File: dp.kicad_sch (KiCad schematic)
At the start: 27 parts, among them J1 DisplayPort_Molex_472720001, U1 74AVC4T245_UQFN, U2 FIN1019MTC, U3 TPD4E05U06QDQARQ1, U4 824012823

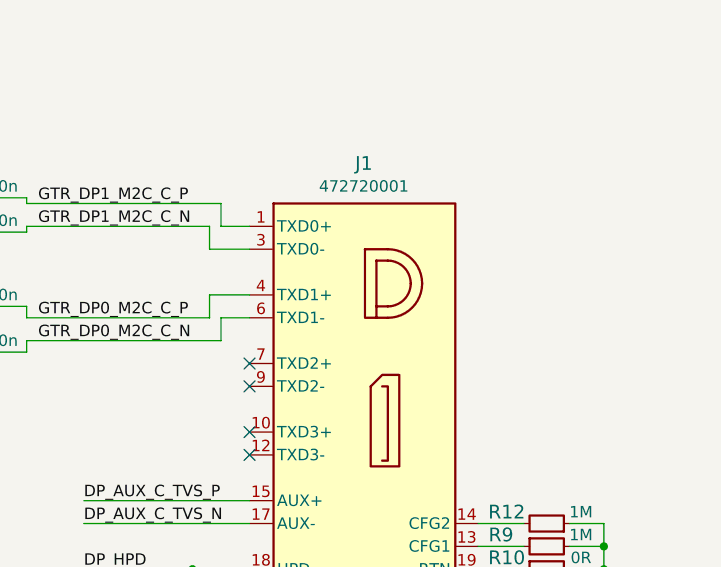
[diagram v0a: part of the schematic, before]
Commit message: removed PoE from schematic
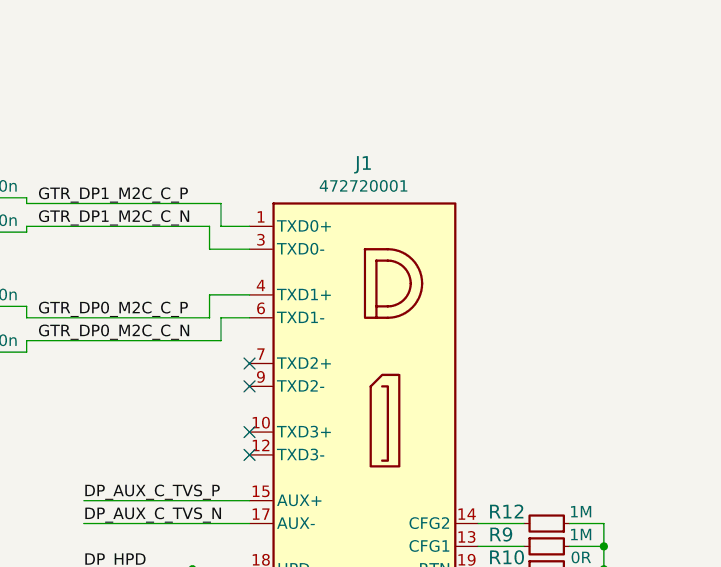
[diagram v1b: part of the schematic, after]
